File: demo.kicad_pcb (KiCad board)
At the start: 2 copper layers, 50 x 25 mm, 5 parts, among them J1 Conn_01x05_Shielded, J2 USB_B_Micro, U1 STM32F103C8Tx

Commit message: update pcb and sch
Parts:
- added C1: 10uF, hardware-demo:C_0805_2012Metric_Pad1.15x1.40mm_HandSolder, F.Cu at (96.3, 147.6)
- added C10: 10pF, hardware-demo:C_0603_1608Metric, F.Cu at (83.9, 130.7)
- added C11: 100nF, hardware-demo:C_0603_1608Metric, F.Cu at (85.8, 130.7)
- added C2: 0.1uF, hardware-demo:C_0603_1608Metric, F.Cu at (95.9, 149.9)
- added C3: 100nF, hardware-demo:C_0603_1608Metric, F.Cu at (88.4, 133.6)
- added C4: 100nF, hardware-demo:C_0603_1608Metric, F.Cu at (71.8, 145.5)
- added C5: 100nF, hardware-demo:C_0603_1608Metric, F.Cu at (82.5, 145.1)
- added C6: 100nF, hardware-demo:C_0603_1608Metric, F.Cu at (88.4, 135.6)
- added C7: 10uF, hardware-demo:C_0805_2012Metric_Pad1.15x1.40mm_HandSolder, F.Cu at (84.4, 148.0)
- added C8: 0.1uF, hardware-demo:C_0603_1608Metric, F.Cu at (84.8, 149.9)
- added C9: 10pF, hardware-demo:C_0603_1608Metric, F.Cu at (77.8, 130.7)
- added D1: LED, hardware-demo:LED_0603_1608Metric, F.Cu at (96.0, 131.7)
- added D2: LED, hardware-demo:LED_0603_1608Metric, F.Cu at (96.1, 130.0)
- added J3: stlink_interface, hardware-demo:PinHeader_1x06_P2.54mm_Horizontal, F.Cu at (68.0, 145.8)
- added R12: 100K, hardware-demo:R_0603_1608Metric, F.Cu at (87.6, 130.7)
- added R13: 4K7, hardware-demo:R_0603_1608Metric, F.Cu at (74.1, 130.7)
- added R14: 4K7, hardware-demo:R_0603_1608Metric, F.Cu at (76.0, 130.7)
- added R3: 100K, hardware-demo:R_0603_1608Metric, F.Cu at (92.7, 136.8)
- added R4: 22, hardware-demo:R_0603_1608Metric, F.Cu at (71.8, 143.3)
- added R5: 22, hardware-demo:R_0603_1608Metric, F.Cu at (71.8, 140.8)
- added R6: 22, hardware-demo:R_0603_1608Metric, F.Cu at (71.8, 138.2)
- added R7: 22, hardware-demo:R_0603_1608Metric, F.Cu at (71.8, 135.7)
- added R8: 100K, hardware-demo:R_0603_1608Metric, F.Cu at (88.4, 137.6)
- added R9: 100R, hardware-demo:R_0603_1608Metric, F.Cu at (78.0, 145.1)
- added U2: AMS1117-3.3, hardware-demo:SOT-223-3_TabPin2, F.Cu at (90.2, 146.2)
- added Y1: Crystal, hardware-demo:Crystal_SMD_3215-2Pin_3.2x1.5mm, F.Cu at (80.9, 131.0)
- J1: value Conn_01x05_Shielded -> download_firmware; footprint Connector_PinHeader_2.54mm:PinHeader_1x05_P2.54mm_Vertical -> hardware-demo:PinHeader_1x04_P2.54mm_Vertical
- J2: footprint Connector_USB:USB_Micro-B_Molex-105133-0031 -> hardware-demo:USB_Micro-B_Amphenol_10103594-0001LF_Horizontal
- R1, R2: value R -> 100R; footprint Resistor_SMD:R_0603_1608Metric -> hardware-demo:R_0603_1608Metric
- U1: footprint Package_QFP:LQFP-48_7x7mm_P0.5mm -> hardware-demo:LQFP-48_7x7mm_P0.5mm
- moved R2 40.3 mm to (92.7, 130.0)
- moved R1 36.2 mm to (92.7, 131.7), turned to 180 degrees
- moved J1 24.3 mm to (72.0, 148.8), turned to 90 degrees
- moved J2 17.9 mm to (97.4, 139.5)
- moved U1 12.5 mm to (80.5, 138.3), turned to 270 degrees
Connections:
- J1 pad 1: Net-(J1-Pad1) -> +3V3
- J1 pad 2: Net-(J1-Pad2) -> /STM_JTMS
- J1 pad 3: Net-(J1-Pad3) -> /STM_JTCK
- J1 pad 4: Net-(J1-Pad4) -> GND
- J2 pad 1: Net-(J2-Pad1) -> +5V
- J2 pad 2: Net-(J2-Pad2) -> /STLINK_USB_DM
- J2 pad 3: Net-(J2-Pad3) -> /STLINK_USB_DP
- J2 pad 5: Net-(J2-Pad5) -> GND
- J2 pad 6: Net-(J2-Pad6) -> GND
- R1 pad 1: Net-(R1-Pad1) -> Net-(D1-Pad2)
- R1 pad 2: Net-(R1-Pad2) -> /LED_STLINK
- R2 pad 2: Net-(R1-Pad1) -> /LED_STLINK
- U1 pad 1: Net-(U1-Pad1) -> +3V3
- U1 pad 10: Net-(R1-Pad2) -> Net-(R13-Pad1)
- U1 pad 11: Net-(U1-Pad11) -> (no net)
- U1 pad 12: Net-(U1-Pad12) -> (no net)
- U1 pad 13: Net-(U1-Pad13) -> (no net)
- U1 pad 14: Net-(U1-Pad14) -> (no net)
- U1 pad 15: Net-(U1-Pad15) -> /T_JTCK
- U1 pad 16: Net-(U1-Pad16) -> (no net)
- U1 pad 17: Net-(U1-Pad17) -> (no net)
- U1 pad 18: Net-(U1-Pad18) -> /T_NRST
- U1 pad 19: Net-(U1-Pad19) -> (no net)
- U1 pad 2: Net-(U1-Pad2) -> (no net)
- U1 pad 20: Net-(U1-Pad20) -> GND
- U1 pad 21: Net-(U1-Pad21) -> (no net)
- U1 pad 22: Net-(U1-Pad22) -> (no net)
- U1 pad 23: Net-(U1-Pad23) -> GND
- U1 pad 24: Net-(U1-Pad24) -> +3V3
- U1 pad 25: Net-(U1-Pad25) -> /T_SWDIO_IN
- U1 pad 26: Net-(U1-Pad26) -> /T_JTCK
- U1 pad 27: Net-(U1-Pad27) -> /T_JTMS
- U1 pad 28: Net-(U1-Pad28) -> (no net)
- U1 pad 29: Net-(U1-Pad29) -> (no net)
- U1 pad 3: Net-(U1-Pad3) -> (no net)
- U1 pad 30: Net-(U1-Pad30) -> /LED_STLINK
- U1 pad 31: Net-(U1-Pad31) -> /SWO
- U1 pad 32: Net-(U1-Pad32) -> /STLINK_USB_DM
- U1 pad 33: Net-(U1-Pad33) -> /STLINK_USB_DP
- U1 pad 34: Net-(U1-Pad34) -> /STM_JTMS
- U1 pad 35: Net-(U1-Pad35) -> GND
- U1 pad 36: Net-(U1-Pad36) -> +3V3
- U1 pad 37: Net-(U1-Pad37) -> /STM_JTCK
- U1 pad 38: Net-(U1-Pad38) -> (no net)
- U1 pad 39: Net-(U1-Pad39) -> (no net)
- U1 pad 4: Net-(U1-Pad4) -> (no net)
- U1 pad 40: Net-(U1-Pad40) -> (no net)
- U1 pad 41: Net-(U1-Pad41) -> (no net)
- U1 pad 42: Net-(U1-Pad42) -> (no net)
- U1 pad 43: Net-(U1-Pad43) -> (no net)
- U1 pad 44: Net-(U1-Pad44) -> /BOOT0
- U1 pad 45: Net-(U1-Pad45) -> (no net)
- U1 pad 46: Net-(U1-Pad46) -> (no net)
- U1 pad 47: Net-(U1-Pad47) -> GND
- U1 pad 48: Net-(U1-Pad48) -> +3V3
- U1 pad 7: Net-(U1-Pad7) -> /NRST
- U1 pad 8: Net-(U1-Pad8) -> GND
- U1 pad 9: Net-(U1-Pad9) -> +3V3
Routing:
- net +3V3: track 0.00 -> 155.7 mm, vias 0 -> 8
- net +5V: track 0.00 -> 14.0 mm
- net /T_JTCK: track 0.00 -> 7.11 mm
- net Net-(C9-Pad2): track 0.00 -> 5.94 mm
- net Net-(C10-Pad2): track 0.00 -> 5.65 mm
- net Net-(J2-Pad4): track 0.00 -> 3.75 mm
- net Net-(J3-Pad5): track 0.00 -> 3.03 mm
- net Net-(J3-Pad4): track 0.00 -> 3.03 mm
- net /SWDIO: track 0.00 -> 3.03 mm
- net /SWCLK: track 0.00 -> 3.03 mm
- net /T_SWDIO_IN: track 0.00 -> 2.89 mm
- net /BOOT0: track 0.00 -> 2.87 mm
- net /T_JTMS: track 0.00 -> 2.65 mm
- net Net-(R13-Pad1): track 0.00 -> 1.89 mm
- net Net-(D2-Pad1): track 0.00 -> 1.77 mm
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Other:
- board size 50 x 25 mm -> 37 x 25 mm
- net class power-3v3 added: clearance 0.2, trace_width 0.5, via_dia 1, via_drill 0.5

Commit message: update pcb and sch
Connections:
- net /STLINK_USB_DM renamed /STLINK_USB_DM-
- net /STLINK_USB_DP renamed /STLINK_USB_DP+
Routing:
- net /LED_STLINK: track 1.73 -> 23.2 mm, vias 0 -> 4
- net /STLINK_USB_DP+: track 0.00 -> 16.1 mm, vias 0 -> 2
- net /STLINK_USB_DM-: track 0.00 -> 16.1 mm, vias 0 -> 2
- net /SWO: track 0.00 -> 15.9 mm, vias 0 -> 2
- net /STM_JTCK: track 0.00 -> 12.1 mm, vias 0 -> 1
- net /STM_JTMS: track 0.00 -> 10.9 mm, vias 0 -> 1
- net /NRST: track 1.76 -> 11.6 mm, vias 0 -> 2
- net /T_JTMS: track 2.65 -> 11.2 mm
- net /T_JTCK: track 7.11 -> 14.9 mm, vias 0 -> 3
- net +3V3: track 155.7 -> 150.3 mm, vias 8 -> 7
- net Net-(R13-Pad1): track 1.89 -> 6.89 mm
- net /T_NRST: track 0.00 -> 3.89 mm
- net GND: vias 0 -> 2
- added copper zone on B.Cu, net GND
- added copper zone on F.Cu, net GND

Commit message: v1.0.0
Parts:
- removed R13, R14: 4K7, hardware-demo:R_0603_1608Metric
- added R10: 22, hardware-demo:R_0402_1005Metric, F.Cu at (98.7, 106.9)
- added R11: 22, hardware-demo:R_0402_1005Metric, F.Cu at (98.7, 104.3)
- added REF**: installHole, hardware-demo:installHole, F.Cu at (96.5, 111.0)
- C1: value 10uF -> 0.1uF; footprint hardware-demo:C_0805_2012Metric_Pad1.15x1.40mm_HandSolder -> hardware-demo:C_0402_1005Metric
- C10, C9: value 10pF -> 100nF; footprint hardware-demo:C_0603_1608Metric -> hardware-demo:C_0402_1005Metric
- C11, C5: footprint hardware-demo:C_0603_1608Metric -> hardware-demo:C_0402_1005Metric
- C2: value 0.1uF -> 10uF; footprint hardware-demo:C_0603_1608Metric -> Capacitor_Tantalum_SMD:CP_EIA-1608-10_AVX-L
- C3: value 100nF -> 10uF; footprint hardware-demo:C_0603_1608Metric -> Capacitor_Tantalum_SMD:CP_EIA-1608-10_AVX-L
- C4: value 100nF -> 0.1uF; footprint hardware-demo:C_0603_1608Metric -> hardware-demo:C_0402_1005Metric
- C6: value 100nF -> 10pF; footprint hardware-demo:C_0603_1608Metric -> hardware-demo:C_0402_1005Metric
- C7: value 10uF -> 10pF; footprint hardware-demo:C_0805_2012Metric_Pad1.15x1.40mm_HandSolder -> hardware-demo:C_0402_1005Metric
- C8: value 0.1uF -> 100nF; footprint hardware-demo:C_0603_1608Metric -> hardware-demo:C_0402_1005Metric
- D1, D2: footprint hardware-demo:LED_0603_1608Metric -> hardware-demo:LED_0402_1005Metric
- J1: value download_firmware -> USB_C_Receptacle_USB2.0; footprint hardware-demo:PinHeader_1x04_P2.54mm_Vertical -> hardware-demo:USB_C_Receptacle_Amphenol_12401610E4-2A
- J2: value USB_B_Micro -> download_firmware; footprint hardware-demo:USB_Micro-B_Amphenol_10103594-0001LF_Horizontal -> Connector_PinHeader_1.27mm:PinHeader_1x04_P1.27mm_Vertical
- J3: footprint hardware-demo:PinHeader_1x06_P2.54mm_Horizontal -> hardware-demo:PinHeader_1x06_P1.27mm_Horizontal
- R1, R2: value 100R -> 100K; footprint hardware-demo:R_0603_1608Metric -> hardware-demo:R_0402_1005Metric
- R12: value 100K -> 22; footprint hardware-demo:R_0603_1608Metric -> hardware-demo:R_0402_1005Metric
- R3: value 100K -> 100R; footprint hardware-demo:R_0603_1608Metric -> hardware-demo:R_0402_1005Metric
- R4, R7: value 22 -> 100R; footprint hardware-demo:R_0603_1608Metric -> hardware-demo:R_0402_1005Metric
- R5, R6: value 22 -> 4K7; footprint hardware-demo:R_0603_1608Metric -> hardware-demo:R_0402_1005Metric
- R8: value 100K -> 5K1; footprint hardware-demo:R_0603_1608Metric -> hardware-demo:R_0402_1005Metric
- R9: value 100R -> 22; footprint hardware-demo:R_0603_1608Metric -> hardware-demo:R_0402_1005Metric
- U1: value STM32F103C8Tx -> XC6220B331MR; footprint hardware-demo:LQFP-48_7x7mm_P0.5mm -> hardware-demo:SOT-23-5
- U2: value AMS1117-3.3 -> STM32F103C8Tx; footprint hardware-demo:SOT-223-3_TabPin2 -> hardware-demo:LQFP-48_7x7mm_P0.5mm
- moved J1 71.4 mm to (129.3, 106.2)
- moved R4 62.3 mm to (119.8, 103.6)
- moved C4 56.8 mm to (117.1, 111.2), turned to 90 degrees
- moved R7 51.8 mm to (115.8, 108.5), turned to 90 degrees
- moved U1 49.3 mm to (121.1, 110.3), turned to 180 degrees
- moved C7 48.5 mm to (104.0, 103.7), turned to 0 degrees
- moved C2 48.0 mm to (118.4, 107.5), turned to 270 degrees
- moved C1 47.6 mm to (120.2, 106.4)
- moved C9 46.8 mm to (115.8, 103.4)
- moved C5 46.7 mm to (102.1, 102.7)
- moved J3 46.4 mm to (96.6, 109.4)
- moved R8 45.9 mm to (122.1, 106.4)
- moved J2 45.4 mm to (122.2, 101.5), turned to 270 degrees
- moved U2 44.7 mm to (110.2, 106.2), turned to 0 degrees
- moved C8 43.5 mm to (104.0, 110.8), turned to 0 degrees
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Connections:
- C10 pad 1: GND -> +3V3
- C10 pad 2: Net-(C10-Pad2) -> GND
- C11 pad 1: /NRST -> +3V3
- C5 pad 1: +3V3 -> /NRST
- C6 pad 1: +3V3 -> GND
- C6 pad 2: GND -> Net-(C6-Pad2)
- C7 pad 1: +3V3 -> GND
- C7 pad 2: GND -> Net-(C7-Pad2)
- C9 pad 1: GND -> +3V3
- C9 pad 2: Net-(C9-Pad2) -> GND
- J2 pad 1: +5V -> +3V3
- J2 pad 2: /STLINK_USB_DM- -> /STM_JTMS
- J2 pad 3: /STLINK_USB_DP+ -> /STM_JTCK
- J2 pad 4: Net-(J2-Pad4) -> GND
- J3 pad 2: /SWDIO -> /SWCLK
- J3 pad 3: /SWCLK -> /SWDIO
- J3 pad 4: Net-(J3-Pad4) -> GND
- J3 pad 6: GND -> Net-(J3-Pad6)
- R1 pad 1: Net-(D1-Pad2) -> /BOOT0
- R1 pad 2: /LED_STLINK -> GND
- R12 pad 1: +3V3 -> /SWO
- R12 pad 2: /NRST -> Net-(J3-Pad6)
- R2 pad 1: Net-(D2-Pad1) -> +3V3
- R2 pad 2: /LED_STLINK -> /NRST
- R3 pad 1: GND -> Net-(D1-Pad2)
- R3 pad 2: Net-(J2-Pad4) -> /LED_STLINK
- R4 pad 1: /T_JTMS -> Net-(D2-Pad1)
- R4 pad 2: /SWDIO -> /LED_STLINK
- R5 pad 1: /T_JTCK -> Net-(R5-Pad1)
- R5 pad 2: /SWCLK -> +3V3
- R6 pad 1: /T_NRST -> GND
- R6 pad 2: Net-(J3-Pad4) -> Net-(R5-Pad1)
- R7 pad 1: /SWO -> /T_SWDIO_IN
- R7 pad 2: Net-(J3-Pad5) -> /T_JTMS
- R8 pad 1: /BOOT0 -> GND
- R8 pad 2: GND -> Net-(J1-PadA5)
- R9 pad 1: /T_SWDIO_IN -> /T_JTCK
- R9 pad 2: /T_JTMS -> /SWCLK
- U1 pad 1: +3V3 -> +5V
- U1 pad 2: (no net) -> GND
- U1 pad 3: (no net) -> +5V
- U1 pad 5: Net-(C10-Pad2) -> +3V3
- U2 pad 1: GND -> +3V3
- U2 pad 2: +3V3 -> (no net)
- U2 pad 3: +5V -> (no net)
- Y1 pad 1: Net-(C9-Pad2) -> Net-(C6-Pad2)
- Y1 pad 2: Net-(C10-Pad2) -> Net-(C7-Pad2)
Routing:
- net +3V3: track 150.3 -> 89.8 mm, vias 7 -> 0
- net GND: track 0.00 -> 35.4 mm, vias 2 -> 4
- net /LED_STLINK: track 23.2 -> 6.78 mm, vias 4 -> 0
- net /T_NRST: track 3.89 -> 16.1 mm, vias 0 -> 2
- net +5V: track 14.0 -> 24.8 mm
- net /BOOT0: track 2.87 -> 12.2 mm, vias 0 -> 2
- net Net-(R5-Pad1): track 0.00 -> 8.17 mm, vias 0 -> 2
- net Net-(J1-PadA5): track 0.00 -> 7.30 mm, vias 0 -> 2
- net Net-(R13-Pad1): track 6.89 -> 0.00 mm
- net Net-(C9-Pad2): track 5.94 -> 0.00 mm
- net /T_JTMS: track 11.2 -> 17.1 mm, vias 0 -> 2
- net Net-(C10-Pad2): track 5.65 -> 0.00 mm
- net Net-(C6-Pad2): track 0.00 -> 4.85 mm
- net /STM_JTCK: track 12.1 -> 7.32 mm, vias 1 -> 2
- net Net-(C7-Pad2): track 0.00 -> 3.99 mm
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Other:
- board size 37 x 25 mm -> 40 x 12.5 mm
- net class Default: trace_width 0.25 -> 0.2
- net class power-3v3: trace_width 0.5 -> 0.3; via_dia 1 -> 0.8; via_drill 0.5 -> 0.4
- rule via_min_drill: 0.3 -> 0.2
- board text added: "3V3"
- board text added: "GND"
- board text added: "NRST"
- board text added: "SWCLK"
- board text added: "SWDIO"
- board text added: "SWO"
- board text added: "designed by wangzefeng"
- board text added: "https://github.com/ZefengWang/hardware-demo"
- board text added: "wangzefeng9@foxmail.com"

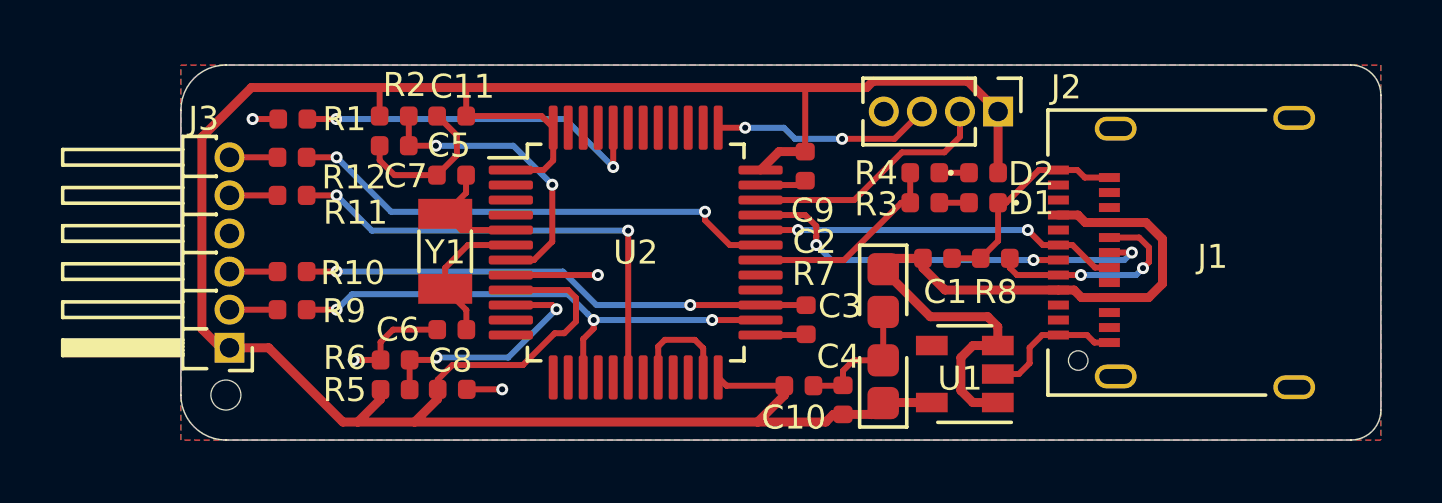
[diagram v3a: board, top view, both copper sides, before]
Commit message: add usb typec-2.0 fp
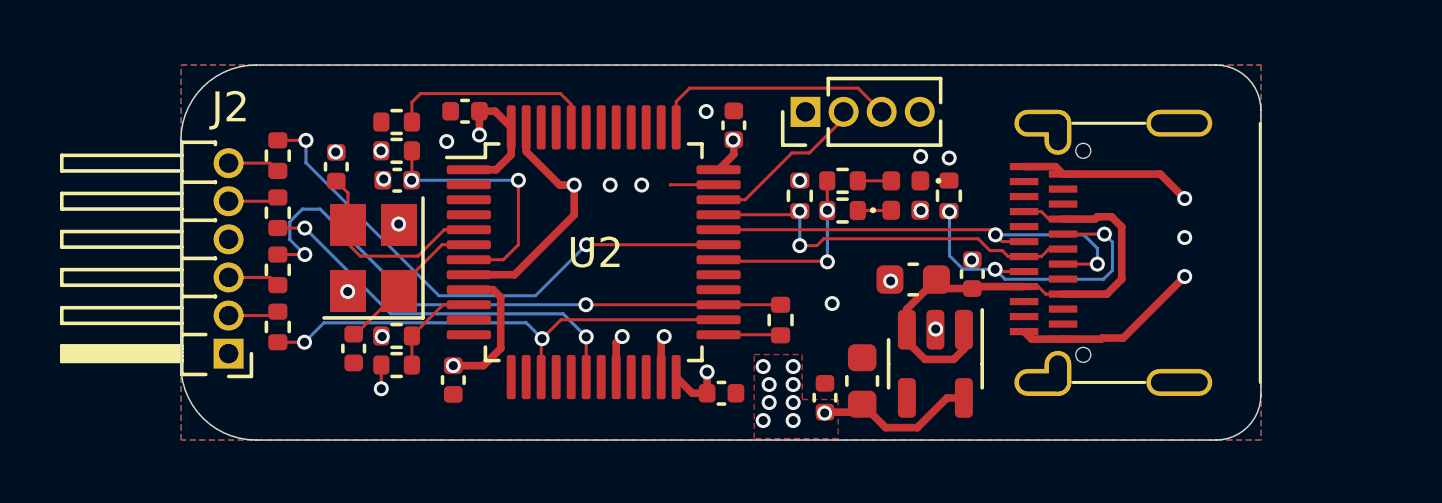
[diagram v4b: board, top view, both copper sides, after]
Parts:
- removed J1: USB_C_Receptacle_USB2.0, hardware-demo:USB_C_Receptacle_Amphenol_12401610E4-2A
- removed REF**: installHole, hardware-demo:installHole
- removed Y1: Crystal, hardware-demo:Crystal_SMD_3215-2Pin_3.2x1.5mm
- added J4: USB_C_Receptacle, selfdefined_library:USB_C_Receptacle_24Pin_Hole_SMD, F.Cu at (123.9, 106.3)
- added R13: 4K7, Resistor_SMD:R_0402_1005Metric, F.Cu at (102.2, 109.0)
- added Y2: 8M, Crystal:Crystal_SMD_3225-4Pin_3.2x2.5mm, F.Cu at (101.4, 106.4)
- C1, C4: value 0.1uF -> 100nF; footprint hardware-demo:C_0402_1005Metric -> Capacitor_SMD:C_0402_1005Metric
- C10, C9: value 100nF -> 10pF; footprint hardware-demo:C_0402_1005Metric -> Capacitor_SMD:C_0402_1005Metric
- C11, C5, C8: footprint hardware-demo:C_0402_1005Metric -> Capacitor_SMD:C_0402_1005Metric
- C2: footprint Capacitor_Tantalum_SMD:CP_EIA-1608-10_AVX-L -> Capacitor_SMD:C_0603_1608Metric
- C3: value 10uF -> 100nF; footprint Capacitor_Tantalum_SMD:CP_EIA-1608-10_AVX-L -> Capacitor_SMD:C_0402_1005Metric
- C6: value 10pF -> 100nF; footprint hardware-demo:C_0402_1005Metric -> Capacitor_SMD:C_0402_1005Metric
- C7: value 10pF -> 10uF; footprint hardware-demo:C_0402_1005Metric -> Capacitor_SMD:C_0603_1608Metric
- D1, D2: footprint hardware-demo:LED_0402_1005Metric -> LED_SMD:LED_0402_1005Metric
- J2: value download_firmware -> Conn_01x06; footprint Connector_PinHeader_1.27mm:PinHeader_1x04_P1.27mm_Vertical -> Connector_PinHeader_1.27mm:PinHeader_1x06_P1.27mm_Horizontal
- J3: value stlink_interface -> Conn_01x04; footprint hardware-demo:PinHeader_1x06_P1.27mm_Horizontal -> Connector_PinHeader_1.27mm:PinHeader_1x04_P1.27mm_Vertical
- R1, R2: value 100K -> 100; footprint hardware-demo:R_0402_1005Metric -> Resistor_SMD:R_0402_1005Metric
- R10: value 22 -> 100; footprint hardware-demo:R_0402_1005Metric -> Resistor_SMD:R_0402_1005Metric
- R11, R9: value 22 -> 100K; footprint hardware-demo:R_0402_1005Metric -> Resistor_SMD:R_0402_1005Metric
- R12: value 22 -> 4K7; footprint hardware-demo:R_0402_1005Metric -> Resistor_SMD:R_0402_1005Metric
- R3: value 100R -> 100K; footprint hardware-demo:R_0402_1005Metric -> Resistor_SMD:R_0402_1005Metric
- R4, R7: value 100R -> 22; footprint hardware-demo:R_0402_1005Metric -> Resistor_SMD:R_0402_1005Metric
- R5, R6: value 4K7 -> 22; footprint hardware-demo:R_0402_1005Metric -> Resistor_SMD:R_0402_1005Metric
- R8: value 5K1 -> 1.5K; footprint hardware-demo:R_0402_1005Metric -> Resistor_SMD:R_0402_1005Metric
- U1: value XC6220B331MR -> Regulator_Linear_XC6220B331MR; footprint hardware-demo:SOT-23-5 -> Package_TO_SOT_SMD:SOT-23-5
- U2: value STM32F103C8Tx -> MCU_ST_STM32F1_STM32F103C8Tx; footprint hardware-demo:LQFP-48_7x7mm_P0.5mm -> Package_QFP:LQFP-48_7x7mm_P0.5mm
- moved J2 26.9 mm to (96.6, 109.6), turned to 180 degrees
- moved R4 22.2 mm to (98.2, 108.7), turned to 90 degrees
- moved J3 20.7 mm to (115.8, 101.6), turned to 90 degrees
- moved R1 18.4 mm to (117.1, 103.9)
- moved R7 18.4 mm to (98.2, 103.0), turned to -90 degrees
- moved C10 17.1 mm to (100.2, 103.4), turned to -90 degrees
- moved R10 16.4 mm to (115.0, 108.5), turned to 90 degrees
- moved C9 16.2 mm to (100.8, 109.5), turned to 90 degrees
- moved C7 15.3 mm to (117.7, 110.5), turned to 90 degrees
- moved R2 15.3 mm to (117.1, 104.8), turned to 180 degrees
- moved C4 13.0 mm to (104.1, 110.5), turned to -90 degrees
- moved C8 12.4 mm to (116.5, 111.1), turned to 90 degrees
- moved C6 11.6 mm to (113.4, 102.0), turned to 90 degrees
- moved R12 7.75 mm to (102.2, 110.0)
- moved R9 7.16 mm to (102.2, 101.9)
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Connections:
- C10 pad 1: +3V3 -> GND
- C10 pad 2: GND -> Net-(U2-PD0)
- C11 pad 1: +3V3 -> /NRST
- C5 pad 1: /NRST -> +3V3
- C6 pad 1: GND -> +3V3
- C6 pad 2: Net-(C6-Pad2) -> GND
- C7 pad 1: GND -> +3V3
- C7 pad 2: Net-(C7-Pad2) -> GND
- C9 pad 1: +3V3 -> GND
- C9 pad 2: GND -> Net-(U2-PD1)
- D1 pad 2: Net-(D1-Pad2) -> Net-(D1-A)
- D2 pad 1: Net-(D2-Pad1) -> Net-(D2-K)
- J2 pad 2: /STM_JTMS -> /SWCLK
- J2 pad 3: /STM_JTCK -> /SWDIO
- J3 pad 2: /SWCLK -> /STM_JTMS
- J3 pad 3: /SWDIO -> /STM_JTCK
- R1 pad 1: /BOOT0 -> Net-(D1-A)
- R1 pad 2: GND -> /LED_STLINK
- R10 pad 1: /T_JTMS -> /T_SWDIO_IN
- R10 pad 2: /SWDIO -> /T_JTMS
- R11 pad 1: /T_NRST -> +3V3
- R11 pad 2: Net-(J3-Pad5) -> /NRST
- R12 pad 1: /SWO -> Net-(U2-PA0)
- R12 pad 2: Net-(J3-Pad6) -> +3V3
- R2 pad 1: +3V3 -> Net-(D2-K)
- R2 pad 2: /NRST -> /LED_STLINK
- R3 pad 1: Net-(D1-Pad2) -> GND
- R3 pad 2: /LED_STLINK -> Net-(J4-CC1)
- R4 pad 1: Net-(D2-Pad1) -> /T_JTCK
- R4 pad 2: /LED_STLINK -> /SWCLK
- R5 pad 1: Net-(R5-Pad1) -> /T_JTMS
- R5 pad 2: +3V3 -> /SWDIO
- R6 pad 1: GND -> /T_NRST
- R6 pad 2: Net-(R5-Pad1) -> Net-(J2-Pin_5)
- R7 pad 1: /T_SWDIO_IN -> /SWO
- R7 pad 2: /T_JTMS -> Net-(J2-Pin_6)
- R8 pad 1: GND -> +3V3
- R8 pad 2: Net-(J1-PadA5) -> /STLINK_USB_DP+
- R9 pad 1: /T_JTCK -> /BOOT0
- R9 pad 2: /SWCLK -> GND
- U1 pad 4: (no net) -> unconnected-(U1-NC-Pad4)
- U2 pad 10: Net-(R5-Pad1) -> Net-(U2-PA0)
- U2 pad 11: (no net) -> unconnected-(U2-PA1-Pad11)
- U2 pad 12: (no net) -> unconnected-(U2-PA2-Pad12)
- U2 pad 13: (no net) -> unconnected-(U2-PA3-Pad13)
- U2 pad 14: (no net) -> unconnected-(U2-PA4-Pad14)
- U2 pad 16: (no net) -> unconnected-(U2-PA6-Pad16)
- U2 pad 17: (no net) -> unconnected-(U2-PA7-Pad17)
- U2 pad 19: (no net) -> unconnected-(U2-PB1-Pad19)
- U2 pad 2: (no net) -> unconnected-(U2-PC13-Pad2)
- U2 pad 21: (no net) -> unconnected-(U2-PB10-Pad21)
- U2 pad 22: (no net) -> unconnected-(U2-PB11-Pad22)
- U2 pad 28: (no net) -> unconnected-(U2-PB15-Pad28)
- U2 pad 29: (no net) -> unconnected-(U2-PA8-Pad29)
- U2 pad 3: (no net) -> unconnected-(U2-PC14-Pad3)
- U2 pad 38: (no net) -> unconnected-(U2-PA15-Pad38)
- U2 pad 39: (no net) -> unconnected-(U2-PB3-Pad39)
- U2 pad 4: (no net) -> unconnected-(U2-PC15-Pad4)
- U2 pad 40: (no net) -> unconnected-(U2-PB4-Pad40)
- U2 pad 41: (no net) -> unconnected-(U2-PB5-Pad41)
- U2 pad 42: (no net) -> unconnected-(U2-PB6-Pad42)
- U2 pad 43: (no net) -> unconnected-(U2-PB7-Pad43)
- U2 pad 45: (no net) -> unconnected-(U2-PB8-Pad45)
- U2 pad 46: (no net) -> unconnected-(U2-PB9-Pad46)
- U2 pad 5: Net-(C7-Pad2) -> Net-(U2-PD0)
- U2 pad 6: Net-(C6-Pad2) -> Net-(U2-PD1)
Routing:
- net +3V3: track 89.8 -> 18.7 mm, vias 0 -> 17
- net Net-(J4-CC1): track 0.00 -> 11.0 mm, vias 0 -> 3
- net GND: track 35.4 -> 24.8 mm, vias 4 -> 21
- net Net-(R5-Pad1): track 8.17 -> 0.00 mm, vias 2 -> 0
- net +5V: track 24.8 -> 17.3 mm
- net Net-(J1-PadA5): track 7.30 -> 0.00 mm, vias 2 -> 0
- net Net-(U2-PD0): track 0.00 -> 6.81 mm
- net /BOOT0: track 12.2 -> 7.01 mm, vias 2 -> 0
- net Net-(U2-PD1): track 0.00 -> 5.13 mm
- net Net-(C6-Pad2): track 4.85 -> 0.00 mm
- net Net-(C7-Pad2): track 3.99 -> 0.00 mm
- net /STLINK_USB_DM-: track 12.1 -> 15.6 mm
- net Net-(U2-PA0): track 0.00 -> 3.30 mm
- net /T_NRST: track 16.1 -> 13.1 mm
- net /T_JTMS: track 17.1 -> 20.1 mm
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- added copper zone on F.Cu, net +3V3
- added copper zone on In2.Cu, net +3V3
- added copper zone on In1.Cu, net GND
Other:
- board size 40 x 12.5 mm -> 36 x 12.5 mm
- copper layers 2 -> 4
- net class Default removed
- net class power-3v3 removed
- rule pad_to_mask_clearance: 0.051 -> 0
- board text removed: "3V3"
- board text removed: "GND"
- board text removed: "NRST"
- board text removed: "SWCLK"
- board text removed: "SWDIO"
- board text removed: "SWO"
- board text removed: "designed by wangzefeng"
- board text removed: "https://github.com/ZefengWang/hardware-demo"
- board text removed: "wangzefeng9@foxmail.com"
